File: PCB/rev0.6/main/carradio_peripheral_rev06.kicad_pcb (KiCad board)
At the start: 4 copper layers, 100 x 100 mm, 213 parts, among them J1 ISO 10487 A (via pigtail), J10 K-line module socket, J12 Display buttons, J13 HDMI in (from VIM3), J14 Display FPC 40P 0.5mm, J18 VIM3 VIN (JST-XH 2P), J2 VIM3 40-pin via 2x20 IDC ribb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, J21 Expansion 2, J22 SWD, J23 Audio module socket, J25 USB module socket, J27 GNSS module socket, J5 VIM3 POWER key lead, J7 BH1750 light sensor, J8 ISO 10487 C1 (via pigtail), Q1 AO3400A, Q10 P-MOSFET -40V, Q11 CSD18543Q3A, Q12 CSD18543Q3A, Q2 P-MOSFET -60V, Q3 2N7002, SW1 BOOTSEL, SW2 RESET, U1 TPS560430XDBVR, U12 TPS55288RPMR, U13 CH334R, U19 AP2112K-3.3, U2 EL817S1(C), U20 RP2350B, U21 W25Q128JVS, U3 EL817S1(C), U4 EL817S1(C), U5 EL817S1(C), U6 LP5907MFX-3.3, Y1 12MHz, Y3 12MHz

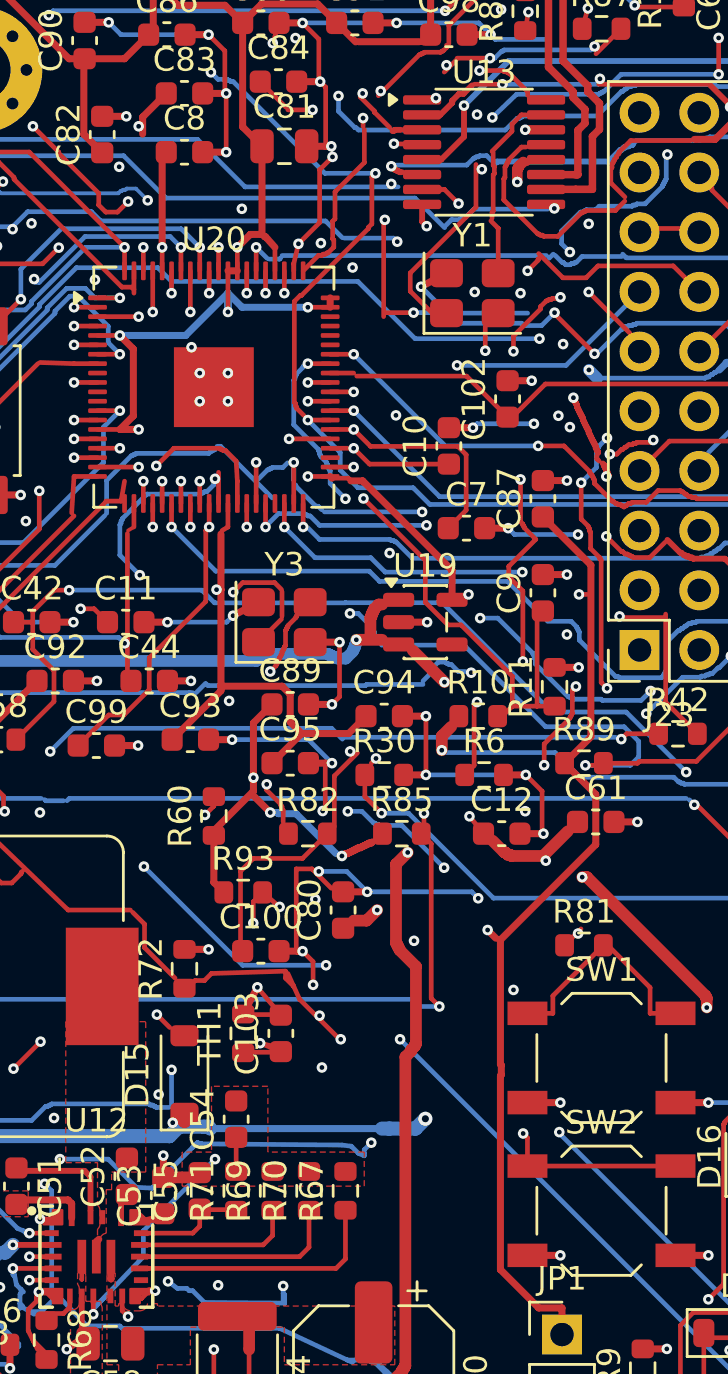
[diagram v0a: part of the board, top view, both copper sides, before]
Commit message: PCB rev 0.6: JLC DFM follow-up (vias near pads, duplicate via, silk clip)
- fixvip.py also moves vias that sit less than 0.1 mm from a same-net
  SMD pad (4 more); dupvia.py merges an overlapping same-net via pair.
- jlcfab.py exports Gerbers with silkscreen clipped at mask openings;
  all four boards' order files regenerated.
- fixnear.py / dfm2.py / outerpar.py: Gerber-style (net-blind) checks;
  the remaining JLC flags are same-net or assembly-rule false
  positives, documented in order/ORDER_INSTRUCTIONS.md.
- Dropped an accidentally committed .kicad_prl.

DRC: 0 unconnected, no errors; schematic parity unchanged.

Co-Authored-By: Claude Opus 5.5 (1M context) <noreply@anthropic.com>
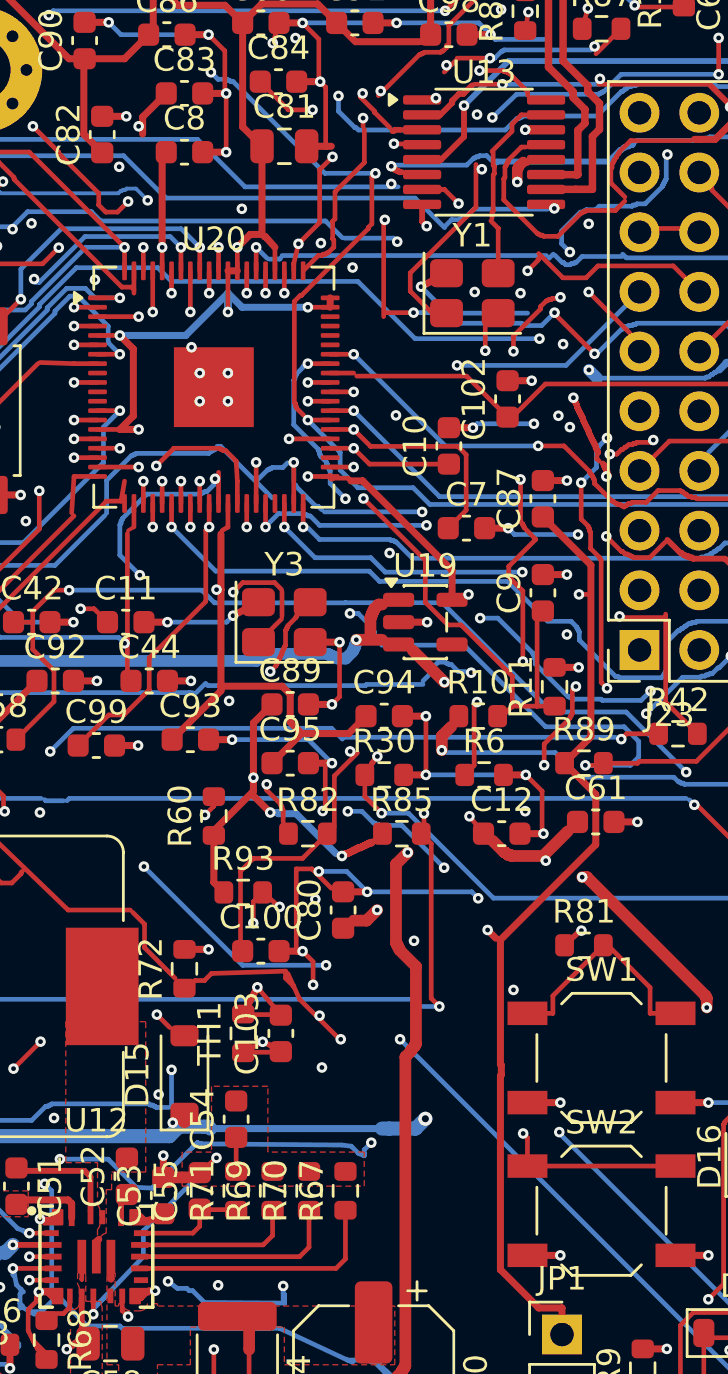
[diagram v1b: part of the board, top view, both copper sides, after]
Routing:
- net /BB_AGND: track 17.6 -> 18.6 mm
- net /MCU_REV_IN: track 69.8 -> 70.8 mm
- net /QSPI_SS: track 78.3 -> 79.1 mm
- net /MCU_TEMP_ADC: track 47.4 -> 48.1 mm
- net GND: vias 156 -> 155
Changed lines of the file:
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@@
 	)
 	(via
-		(at 46 19.75)
-		(size 0.45)
-		(drill 0.2)
-		(layers "F.Cu" "B.Cu")
-		(net "GND")
-	)
-	(via
 		(at 95.555 25.645)
 		(size 0.45)
@@
 	)
 	(segment
+		(start 40.4 63.425)
+		(end 41.111546 62.795554)
+		(width 0.2)
+		(locked yes)
+		(layer "F.Cu")
+		(net "/BB_AGND")
+	)
+	(segment
 		(start 33.45 68.8)
 		(end 33.45 68.9)
@@
 	)
 	(via
-		(at 41.05 62.85)
+		(at 41.111546 62.795554)
 		(size 0.45)
 		(drill 0.2)
@@
 	)
 	(segment
-		(start 41.05 62.85)
+		(start 41.111546 62.795554)
 		(end 38 65.9)
 		(width 0.2)
@@
 	)
 	(segment
+		(start 55.925 53.75)
+		(end 56.641875 53.12663)
+		(width 0.2)
+		(locked yes)
+		(layer "F.Cu")
+		(net "/QSPI_SS")
+	)
+	(segment
 		(start 24.5087 34.2925)
 		(end 22.3961 32.1799)
@@
 	)
 	(via
-		(at 56.5 53.25)
+		(at 56.641875 53.12663)
 		(size 0.45)
 		(drill 0.2)
@@
 	)
 	(segment
-		(start 56.5 53.1)
-		(end 56.5 53.25)
+		(start 56.641875 53.12663)
+		(end 56.641875 53.12663)
 		(width 0.2)
 		(layer "In2.Cu")
@@
 	(segment
 		(start 56.6 53)
-		(end 56.5 53.1)
+		(end 56.641875 53.12663)
 		(width 0.2)
 		(layer "In2.Cu")
@@
 	)
 	(segment
-		(start 42.970212 57.916567)
+		(start 43.076367 57.856366)
 		(end 43.65 58.075)
 		(width 0.2)
@@
 	(segment
 		(start 43.85 58.275)
-		(end 42.970212 57.916567)
+		(end 43.076367 57.856366)
 		(width 0.2)
 		(locked yes)
@@
 	)
 	(segment
+		(start 42.25 58.325)
+		(end 43.076367 57.856366)
+		(width 0.2)
+		(locked yes)
+		(layer "F.Cu")
+		(net "/MCU_TEMP_ADC")
+	)
+	(segment
 		(start 43.075 51.5)
 		(end 42.6789 51.8961)
@@
 	)
 	(via
-		(at 42.970212 57.916567)
+		(at 43.076367 57.856366)
 		(size 0.45)
 		(drill 0.2)
@@
 	)
 	(segment
-		(start 42.970212 57.916567)
-		(end 42.970212 57.916567)
+		(start 43.076367 57.856366)
+		(end 43.076367 57.856366)
 		(width 0.2)
 		(layer "In2.Cu")
@@
 	(segment
 		(start 43.8097 57.6403)
-		(end 42.970212 57.916567)
+		(end 43.076367 57.856366)
 		(width 0.2)
 		(layer "In2.Cu")
@@
 	)
 	(segment
-		(start 47.9 45.8)
+		(start 47.958426 45.713898)
 		(end 47.7 46)
 		(width 0.2)
@@
 		(net "/MCU_REV_IN")
 	)
+	(segment
+		(start 47.425 46.5)
+		(end 47.958426 45.713898)
+		(width 0.2)
+		(locked yes)
+		(layer "F.Cu")
+		(net "/MCU_REV_IN")
+	)
 	(via
 		(at 91.0973 56.0219)
@@
 	)
 	(via
-		(at 47.9 45.8)
+		(at 47.958426 45.713898)
 		(size 0.45)
 		(drill 0.2)
@@
 	(segment
 		(start 48 41.15)
-		(end 48 45.7)
+		(end 47.958426 45.713898)
 		(width 0.2)
 		(locked yes)
@@
 	)
 	(segment
-		(start 48 45.7)
-		(end 47.9 45.8)
+		(start 47.958426 45.713898)
+		(end 47.958426 45.713898)
 		(width 0.2)
 		(locked yes)

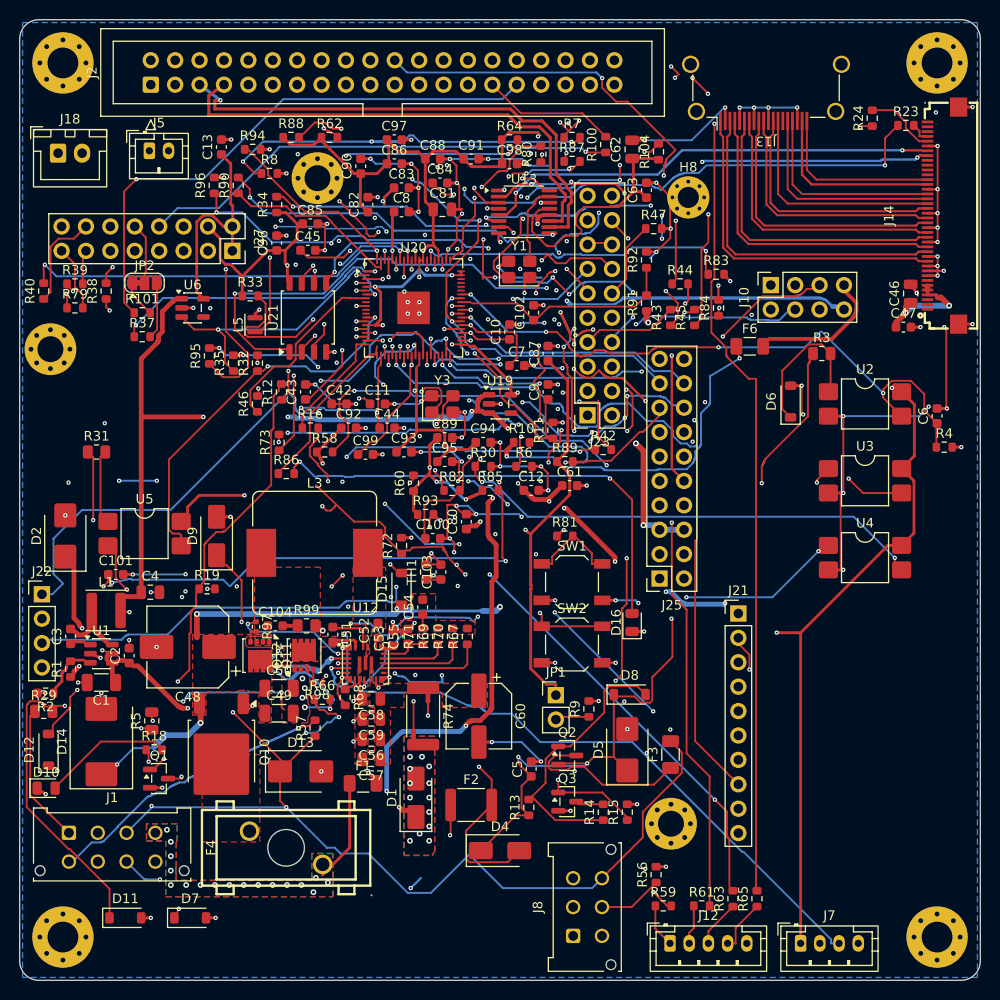
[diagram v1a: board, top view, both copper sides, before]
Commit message: PCB rev 0.6: remove same-net trace slivers flagged by JLC DFM
JLC's Gerber DFM reported a 0.01 mm "trace spacing" on B.Cu: two
parallel 0.2 mm pieces of DAC_XSMT running side by side, a leftover
of the grid routers. fixpar.py removes such slivers on F.Cu/B.Cu:
redundant duplicate pieces are deleted when the net stays connected
(383), otherwise the shorter piece moves onto the longer one's line
(41). fixjoint.py fills the notch where two pieces continue each other
with a small offset (18). Wide copper per net unchanged; +5V_AON
re-widened.

DRC: 0 unconnected, no errors; schematic parity unchanged.

Co-Authored-By: Claude Opus 5.5 (1M context) <noreply@anthropic.com>
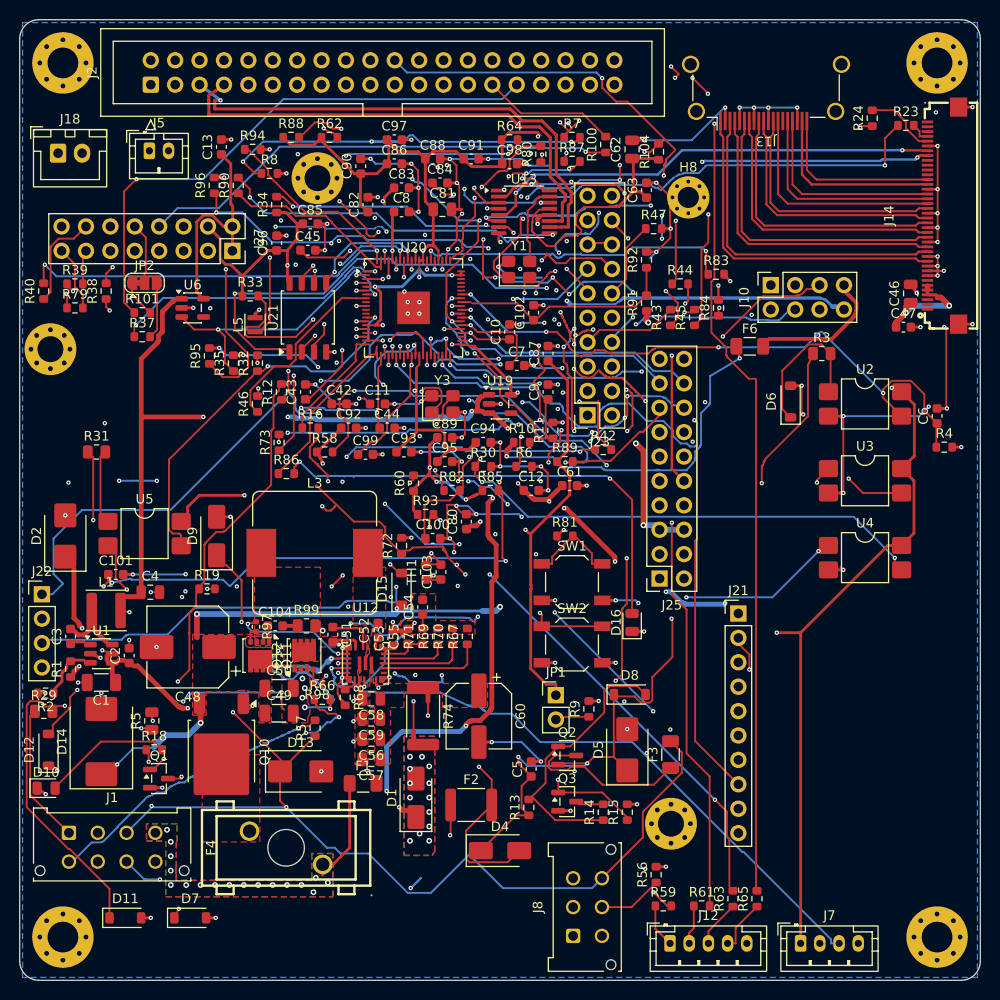
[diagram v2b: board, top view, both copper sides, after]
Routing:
- net GND: track 668.4 -> 660.6 mm
- net /ISO_A5: track 30.4 -> 22.9 mm
- net /HUB2_UP_DM: track 46.5 -> 44.1 mm
- net /DAC_XSMT: track 101.8 -> 100.7 mm
- net /MCU_ACC_IN: track 65.5 -> 64.7 mm
- net /+3V3_MCU: track 371.0 -> 370.2 mm
- net /MCU_BTN_VOLDN: track 115.2 -> 114.5 mm
- net /MCU_BL_EN: track 104.1 -> 103.5 mm
- net /EXP_GP32: track 40.4 -> 39.8 mm
- net /ACC_P: track 150.8 -> 150.2 mm
- net /MCU_XTAL_R: track 19.0 -> 18.4 mm
- net /HUB_3V3: track 25.7 -> 25.2 mm
- net /VIM3_PWR_EN: track 90.2 -> 89.7 mm
- net /+5V_AON: track 181.1 -> 180.6 mm
